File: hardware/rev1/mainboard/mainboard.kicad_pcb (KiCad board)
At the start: 2 copper layers, 40 x 108 mm, 59 parts, among them J1 CONN_05X2SHD, J2 Conn_01x10_Female, J3 Conn_01x10_Female, U1 LM1117-5.0, U2 LM1117-3.3, U3 SAMD51J, U4 OPA197, U5 W25Q32FVSS, U6 AD5685xRUZ, U7 SN74AHCT125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

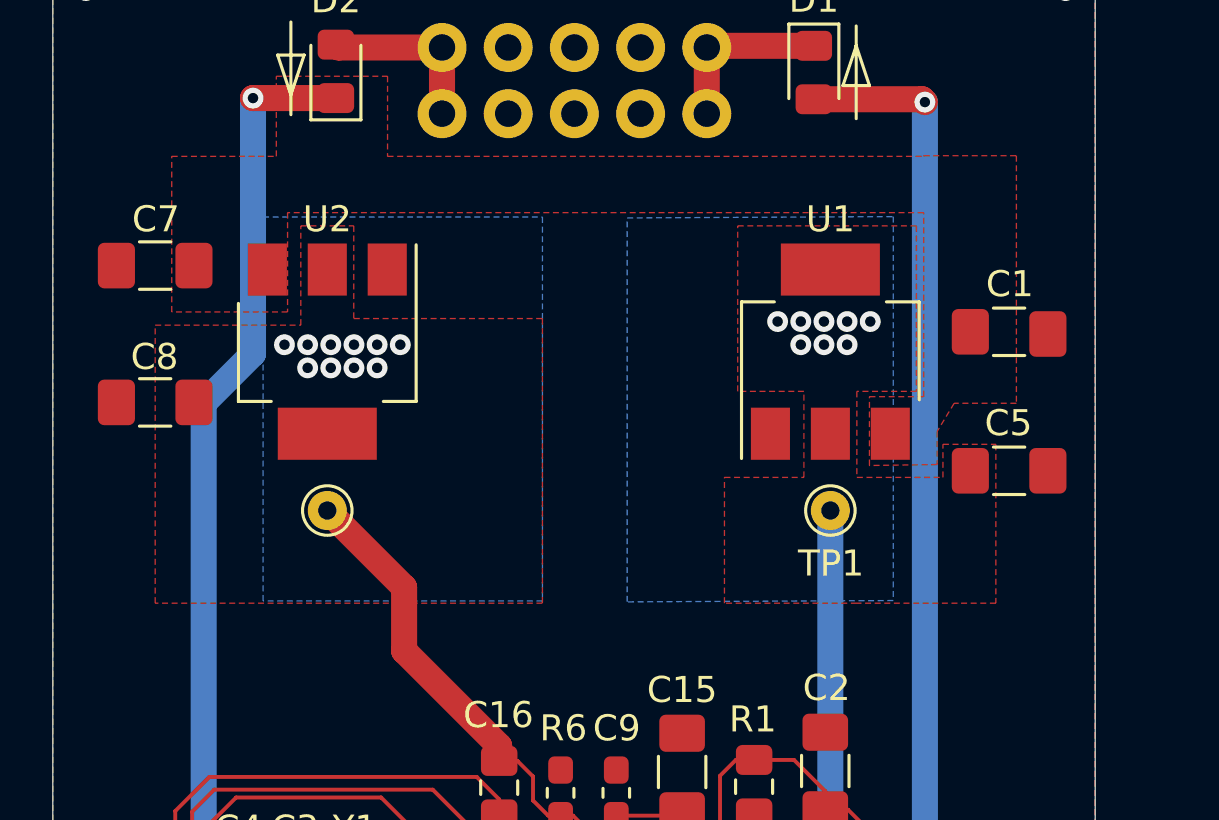
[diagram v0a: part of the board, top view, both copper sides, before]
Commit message: Switch 3v3 regulator to TPS796
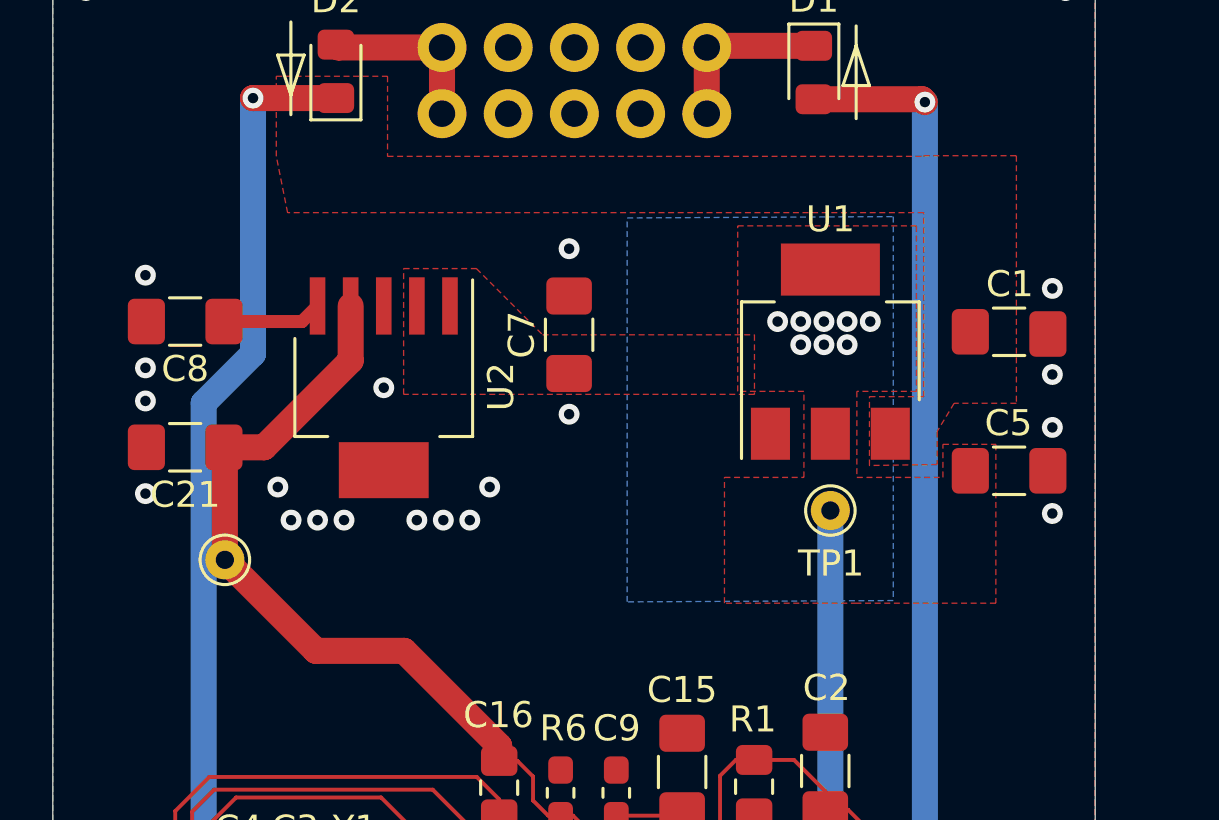
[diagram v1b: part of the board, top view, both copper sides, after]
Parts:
- added C21: 1uF, Capacitor_SMD:C_1206_3216Metric_Pad1.42x1.75mm_HandSolder, F.Cu at (122.1, 71.8)
- C7: value 22uF -> 4.7uF
- C8: value 22uF -> 0.1uF
- U2: value LM1117-3.3 -> TPS79633; footprint Package_TO_SOT_SMD:SOT-223-3_TabPin2 -> Package_TO_SOT_SMD:SOT-223-6_TabPin3
- moved C7 16.1 mm to (136.8, 67.5), turned to 90 degrees
- moved TP2 4.36 mm to (123.6, 76.2)
- moved C8 3.31 mm to (122.1, 67.0)
- moved U2 2.57 mm to (129.7, 69.6)
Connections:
- C7 pad 1: +12V -> +5V
- C8 pad 1: VDDIO -> Net-(C8-Pad1)
- U2 pad 1: GND -> +5V
- U2 pad 2: VDDIO -> +5V
- U2 pad 3: +12V -> GND
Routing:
- net VDDIO: track 189.9 -> 204.3 mm, vias 10 -> 0
- net Net-(C8-Pad1): track 0.00 -> 3.84 mm
- net GND: vias 30 -> 49
- removed copper zone on B.Cu, net VDDIO
- removed copper zone on F.Cu, net VDDIO

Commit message: Replace voltage reference buffer with OPA388
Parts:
- U4: value OPA197 -> OPA388
- moved TP2 4.85 mm to (127.2, 79.5)
- moved U4 0.31 mm to (129.4, 116.8)
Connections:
- C12 pad 2: +12V -> VDDIO
- U4 pad 5: +12V -> VDDIO
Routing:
- net VDDIO: track 204.3 -> 216.0 mm
- net +12V: track 105.9 -> 99.5 mm, vias 3 -> 2
- net MIDVREF: track 44.8 -> 44.1 mm
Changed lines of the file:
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@@
     (thickness 1.6)
     (drawings 36)
-    (tracks 690)
+    (tracks 689)
     (zones 0)
     (modules 60)
@@
   )
   (setup
-    (last_trace_width 0.5)
+    (last_trace_width 0.15)
     (user_trace_width 0.15)
     (user_trace_width 0.5)
@@
   )
   (module TestPoint:TestPoint_THTPad_D1.5mm_Drill0.7mm (layer F.Cu)
-    (at 123.604 76.162 90)
+    (at 127.16 79.464 90)
     (descr "THT pad as test Point, diameter 1.5mm, hole diameter 0.7mm")
     (tags "test point THT pad")
@@
       (net 1 GND))
     (pad 2 smd roundrect (at 0.875 0 270) (size 1.05 0.95) (layers F.Cu F.Paste F.Mask) (roundrect_rratio 0.25)
-      (net 2 +12V))
+      (net 6 VDDIO))
     (model ${KISYS3DMOD}/Capacitor_SMD.3dshapes/C_0603_1608Metric.wrl
       (at (xyz 0 0 0))
@@
       (net 91 MIDVREF))
   )
-  (module Package_TO_SOT_SMD:TSOT-23-5_HandSoldering (layer F.Cu)
-    (at 129.7234 116.9289 180)
-    (descr "5-pin TSOT23 package, http://cds.linear.com/docs/en/packaging/SOT_5_05-08-1635.pdf")
-    (tags "TSOT-23-5 Hand-soldering")
-    (attr smd)
-    (fp_text reference U4 (at 3.5433 -0.0127 90) (layer F.SilkS)
-      (effects (font (size 1 1) (thickness 0.15)))
-    )
-    (fp_text value OPA197 (at 0 2.5) (layer F.Fab)
-      (effects (font (size 1 1) (thickness 0.15)))
-    )
-    (fp_text user %R (at 0 0 90) (layer F.Fab)
-      (effects (font (size 0.5 0.5) (thickness 0.075)))
-    )
-    (fp_line (start -0.88 1.56) (end 0.88 1.56) (layer F.SilkS) (width 0.12))
-    (fp_line (start 0.88 -1.51) (end -1.55 -1.51) (layer F.SilkS) (width 0.12))
-    (fp_line (start -0.88 -1) (end -0.43 -1.45) (layer F.Fab) (width 0.1))
-    (fp_line (start 0.88 -1.45) (end -0.43 -1.45) (layer F.Fab) (width 0.1))
-    (fp_line (start -0.88 -1) (end -0.88 1.45) (layer F.Fab) (width 0.1))
-    (fp_line (start 0.88 1.45) (end -0.88 1.45) (layer F.Fab) (width 0.1))
-    (fp_line (start 0.88 -1.45) (end 0.88 1.45) (layer F.Fab) (width 0.1))
-    (fp_line (start -2.96 -1.7) (end 2.96 -1.7) (layer F.CrtYd) (width 0.05))
-    (fp_line (start -2.96 -1.7) (end -2.96 1.7) (layer F.CrtYd) (width 0.05))
-    (fp_line (start 2.96 1.7) (end 2.96 -1.7) (layer F.CrtYd) (width 0.05))
-    (fp_line (start 2.96 1.7) (end -2.96 1.7) (layer F.CrtYd) (width 0.05))
-    (pad 1 smd rect (at -1.71 -0.95 180) (size 2 0.65) (layers F.Cu F.Paste F.Mask)
-      (net 91 MIDVREF))
-    (pad 2 smd rect (at -1.71 0 180) (size 2 0.65) (layers F.Cu F.Paste F.Mask)
-      (net 1 GND))
-    (pad 3 smd rect (at -1.71 0.95 180) (size 2 0.65) (layers F.Cu F.Paste F.Mask)
-      (net 66 "Net-(R2-Pad2)"))
-    (pad 4 smd rect (at 1.71 0.95 180) (size 2 0.65) (layers F.Cu F.Paste F.Mask)
-      (net 91 MIDVREF))
-    (pad 5 smd rect (at 1.71 -0.95 180) (size 2 0.65) (layers F.Cu F.Paste F.Mask)
-      (net 2 +12V))
-    (model ${KISYS3DMOD}/Package_TO_SOT_SMD.3dshapes/TSOT-23-5.wrl
-      (at (xyz 0 0 0))
-      (scale (xyz 1 1 1))
-      (rotate (xyz 0 0 0))
-    )
-  )
   (module Resistor_SMD:R_1206_3216Metric_Pad1.42x1.75mm_HandSolder (layer F.Cu)
     (at 129.2174 123.2917)
@@
     )
   )
+  (module Package_TO_SOT_SMD:TSOT-23-5_HandSoldering (layer F.Cu)
+    (at 129.446 116.802 180)
+    (descr "5-pin TSOT23 package, http://cds.linear.com/docs/en/packaging/SOT_5_05-08-1635.pdf")
+    (tags "TSOT-23-5 Hand-soldering")
+    (attr smd)
+    (fp_text reference U4 (at 0 -2.45) (layer F.SilkS)
+      (effects (font (size 1 1) (thickness 0.15)))
+    )
+    (fp_text value OPA388 (at 0 2.5) (layer F.Fab)
+      (effects (font (size 1 1) (thickness 0.15)))
+    )
+    (fp_text user %R (at 0 0 90) (layer F.Fab)
+      (effects (font (size 0.5 0.5) (thickness 0.075)))
+    )
+    (fp_line (start -0.88 1.56) (end 0.88 1.56) (layer F.SilkS) (width 0.12))
+    (fp_line (start 0.88 -1.51) (end -1.55 -1.51) (layer F.SilkS) (width 0.12))
+    (fp_line (start -0.88 -1) (end -0.43 -1.45) (layer F.Fab) (width 0.1))
+    (fp_line (start 0.88 -1.45) (end -0.43 -1.45) (layer F.Fab) (width 0.1))
+    (fp_line (start -0.88 -1) (end -0.88 1.45) (layer F.Fab) (width 0.1))
+    (fp_line (start 0.88 1.45) (end -0.88 1.45) (layer F.Fab) (width 0.1))
+    (fp_line (start 0.88 -1.45) (end 0.88 1.45) (layer F.Fab) (width 0.1))
+    (fp_line (start -2.96 -1.7) (end 2.96 -1.7) (layer F.CrtYd) (width 0.05))
+    (fp_line (start -2.96 -1.7) (end -2.96 1.7) (layer F.CrtYd) (width 0.05))
+    (fp_line (start 2.96 1.7) (end 2.96 -1.7) (layer F.CrtYd) (width 0.05))
+    (fp_line (start 2.96 1.7) (end -2.96 1.7) (layer F.CrtYd) (width 0.05))
+    (pad 1 smd rect (at -1.71 -0.95 180) (size 2 0.65) (layers F.Cu F.Paste F.Mask)
+      (net 91 MIDVREF))
+    (pad 2 smd rect (at -1.71 0 180) (size 2 0.65) (layers F.Cu F.Paste F.Mask)
+      (net 1 GND))
+    (pad 3 smd rect (at -1.71 0.95 180) (size 2 0.65) (layers F.Cu F.Paste F.Mask)
+      (net 66 "Net-(R2-Pad2)"))
+    (pad 4 smd rect (at 1.71 0.95 180) (size 2 0.65) (layers F.Cu F.Paste F.Mask)
+      (net 91 MIDVREF))
+    (pad 5 smd rect (at 1.71 -0.95 180) (size 2 0.65) (layers F.Cu F.Paste F.Mask)
+      (net 6 VDDIO))
+    (model ${KISYS3DMOD}/Package_TO_SOT_SMD.3dshapes/TSOT-23-5.wrl
+      (at (xyz 0 0 0))
+      (scale (xyz 1 1 1))
+      (rotate (xyz 0 0 0))
+    )
+  )
   (gr_text "TRANS RIGHTS" (at 210.312 142.748) (layer F.SilkS)
     (effects (font (size 1 1) (thickness 0.15)))
@@
   (via (at 120.556 65.24) (size 0.8) (drill 0.4) (layers F.Cu B.Cu) (net 1))
   (via (at 120.556 68.796) (size 0.8) (drill 0.4) (layers F.Cu B.Cu) (net 1))
-  (segment (start 125.368 117.8789) (end 125.3312 117.8421) (width 0.15) (layer F.Cu) (net 2))
-  (segment (start 128.2364 117.8789) (end 125.368 117.8789) (width 0.15) (layer F.Cu) (net 2))
+  (segment (start 125.368 117.8789) (end 125.3312 117.8421) (width 0.15) (layer F.Cu) (net 6))
+  (segment (start 128.2364 117.8789) (end 125.368 117.8789) (width 0.15) (layer F.Cu) (net 6))
   (segment (start 124.6852 58.4438) (end 124.6835 58.4455) (width 1) (layer F.Cu) (net 2))
   (via (at 124.6835 58.4455) (size 0.8) (drill 0.4) (layers F.Cu B.Cu) (net 2))
@@
   (segment (start 126.7954 143.7678) (end 126.2837 143.2561) (width 0.5) (layer F.Cu) (net 2))
   (segment (start 129.7127 143.7678) (end 126.7954 143.7678) (width 0.5) (layer F.Cu) (net 2))
-  (via (at 124.9121 119.1388) (size 0.8) (drill 0.4) (layers F.Cu B.Cu) (net 2))
-  (segment (start 125.128 118.9229) (end 124.9121 119.1388) (width 0.5) (layer F.Cu) (net 2))
-  (segment (start 125.128 117.8294) (end 125.128 118.9229) (width 0.5) (layer F.Cu) (net 2))
-  (segment (start 122.8293 119.1388) (end 124.9121 119.1388) (width 0.5) (layer B.Cu) (net 2))
   (segment (start 122.7912 70.146802) (end 122.7912 119.1007) (width 1) (layer B.Cu) (net 2))
   (segment (start 122.7912 119.1007) (end 122.8293 119.1388) (width 0.5) (layer B.Cu) (net 2))
@@
   (segment (start 148.369 124.676) (end 149.6784 125.9854) (width 0.15) (layer F.Cu) (net 6))
   (segment (start 122.9944 105.4228) (end 120.2512 102.6796) (width 0.15) (layer F.Cu) (net 6))
-  (segment (start 124.3025 110.9092) (end 122.9944 109.6011) (width 0.15) (layer F.Cu) (net 6))
   (segment (start 126.4488 110.9092) (end 124.3025 110.9092) (width 0.15) (layer F.Cu) (net 6))
   (segment (start 126.8933 111.3537) (end 126.4488 110.9092) (width 0.15) (layer F.Cu) (net 6))
@@
   (segment (start 123.604 71.8805) (end 123.5675 71.844) (width 1) (layer F.Cu) (net 6))
   (segment (start 123.604 76.162) (end 123.604 71.8805) (width 1) (layer F.Cu) (net 6))
+  (segment (start 125.128 117.8294) (end 124.1234 117.8294) (width 0.15) (layer F.Cu) (net 6))
+  (segment (start 123.604 117.31) (end 123.604 110.198) (width 0.15) (layer F.Cu) (net 6))
+  (segment (start 123.604 110.198) (end 122.9944 109.6011) (width 0.15) (layer F.Cu) (net 6))
+  (segment (start 124.1234 117.8294) (end 123.604 117.31) (width 0.15) (layer F.Cu) (net 6))
+  (segment (start 124.3025 110.9092) (end 123.604 110.198) (width 0.15) (layer F.Cu) (net 6))
   (segment (start 127.9594 56.4896) (end 127.8636 56.3938) (width 1) (layer F.Cu) (net 7))
   (segment (start 131.9352 59.0424) (end 131.9352 56.5024) (width 1) (layer F.Cu) (net 7))
@@
   (segment (start 138.75 105.0215) (end 137.451789 106.319711) (width 0.15) (layer F.Cu) (net 89))
   (segment (start 137.451789 106.319711) (end 137.451789 115.554668) (width 0.15) (layer F.Cu) (net 89))
-  (segment (start 128.9114 115.9789) (end 128.2364 115.9789) (width 0.15) (layer F.Cu) (net 91))
   (segment (start 128.0134 115.5039) (end 128.9251 114.5922) (width 0.15) (layer F.Cu) (net 91))
   (segment (start 128.0134 115.9789) (end 128.0134 115.5039) (width 0.15) (layer F.Cu) (net 91))

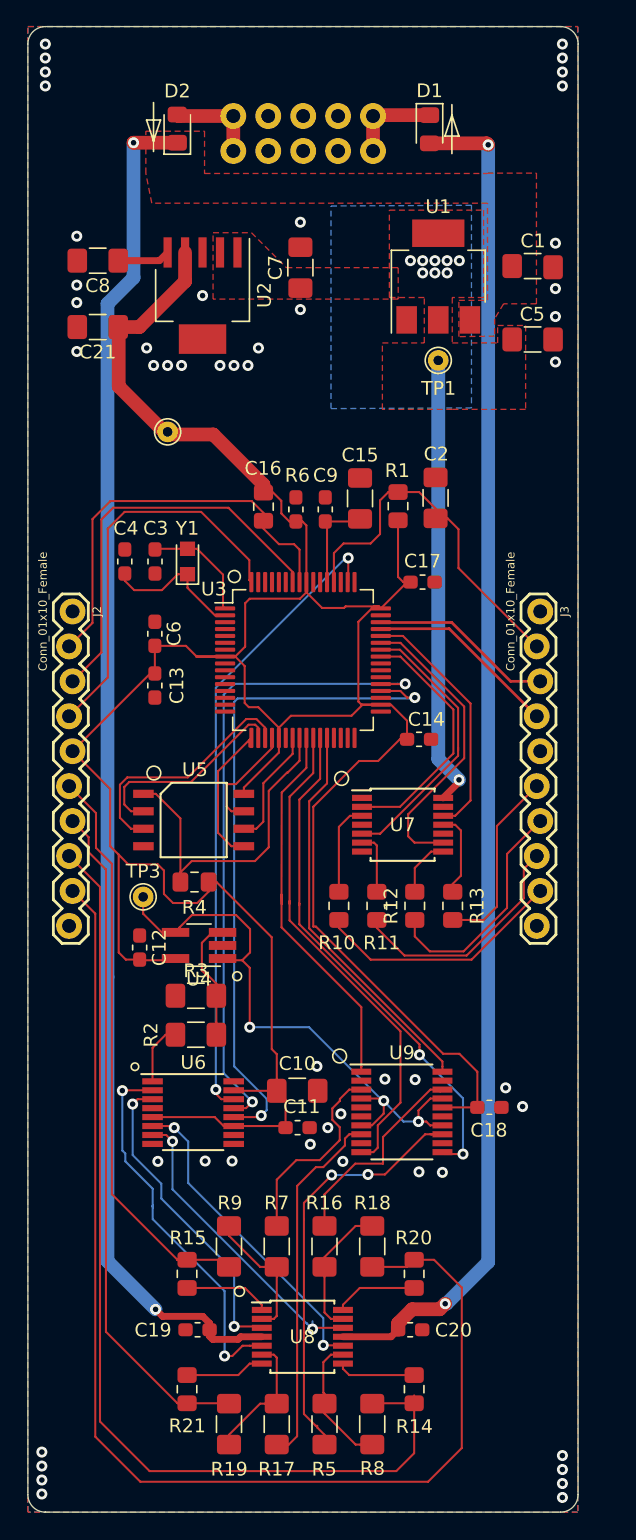
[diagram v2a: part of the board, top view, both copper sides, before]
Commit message: Re-route the +12v trace and do a bunch of ground stitching
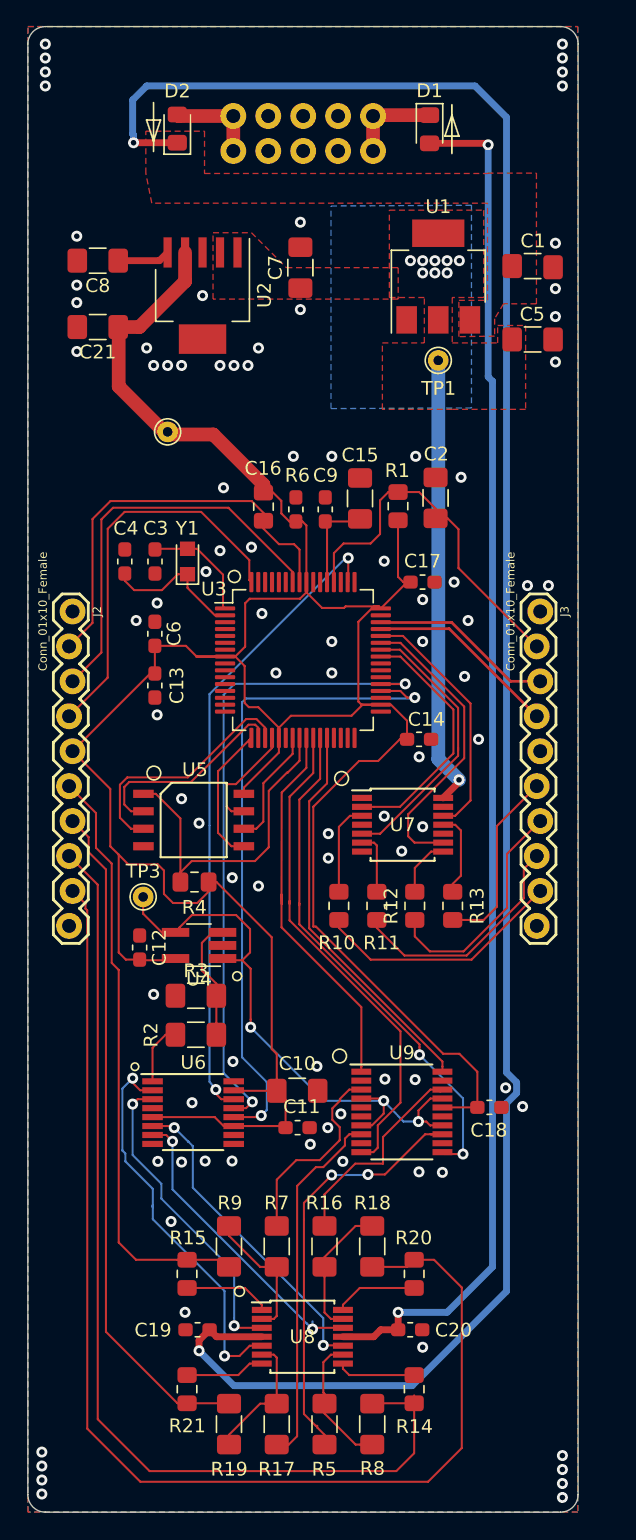
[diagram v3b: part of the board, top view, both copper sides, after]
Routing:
- net +12V: track 99.5 -> 152.9 mm
- net CV_A: track 41.7 -> 44.2 mm
- net -12V: track 98.6 -> 99.7 mm
- net DAC_OUT_B: track 27.9 -> 28.9 mm
- net SCLK: track 49.2 -> 48.4 mm
- net GND: vias 49 -> 90

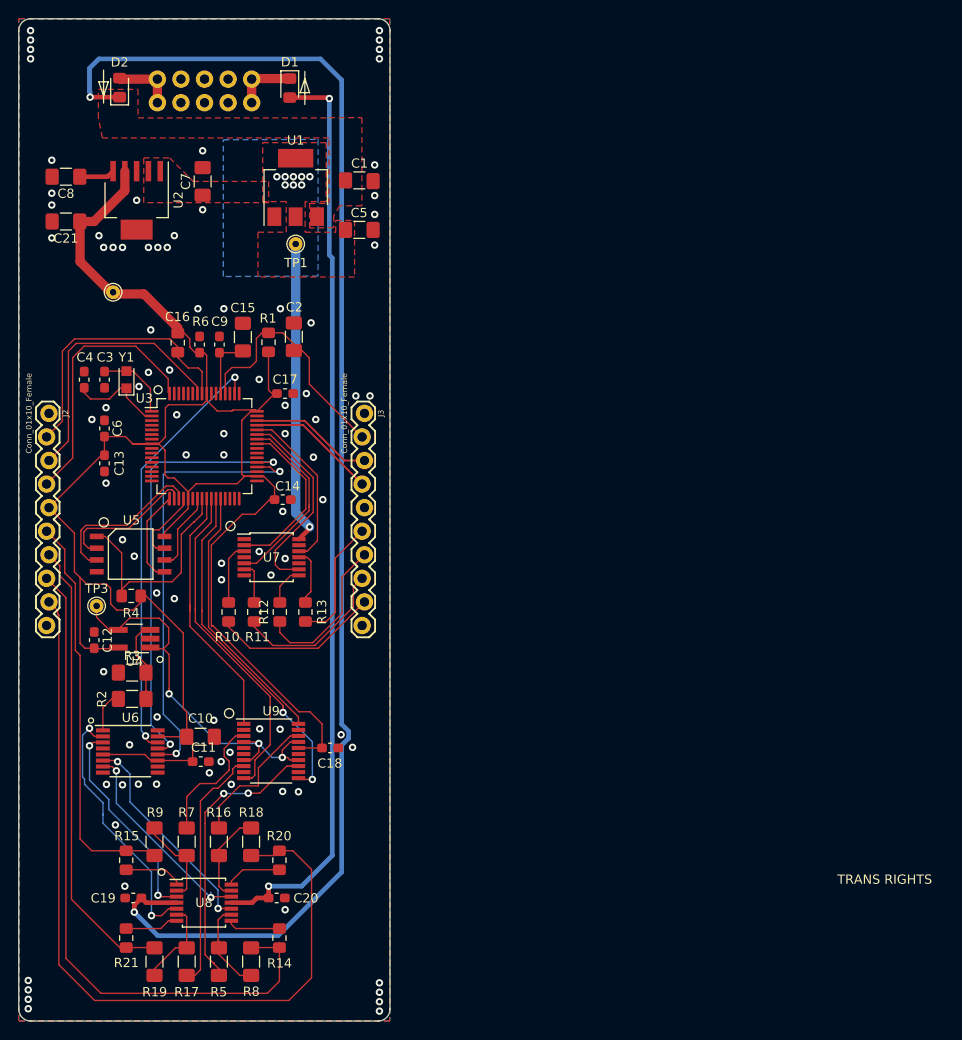
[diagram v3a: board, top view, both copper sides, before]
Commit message: Finish up mainboard - place silkscreen, add branding, etc.
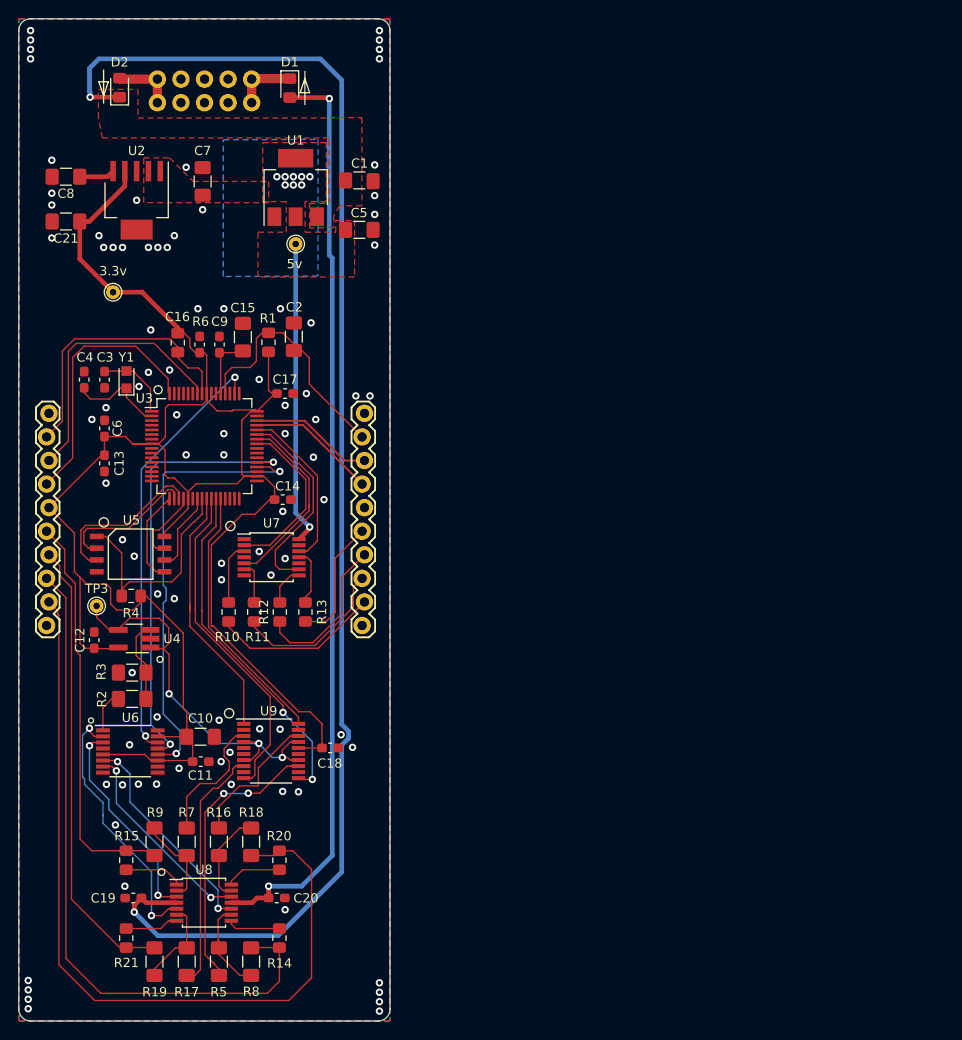
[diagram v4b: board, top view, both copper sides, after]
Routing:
- net DAC_OUT_D: track 22.3 -> 21.8 mm
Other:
- board text added: "Alethea Flowers CC-BY-SA 4.0 v4 2020/1/13 wntr.dev"
- board text removed: "Alethea Flowers CC-BY-SA 4.0 v4 2020/1/11 thea.codes"
